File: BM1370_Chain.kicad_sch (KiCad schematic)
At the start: 30 parts, among them J6 Conn_01x06, U13 25MHz, U14 TXU0304PW, U15 MCP1824T-0802E, U16 MCP1824T-1202E

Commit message: board stakup updated and schematic is updated
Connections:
- net BM1370-1/BI: no longer R47.2
- net BM1370-1/CLKI: now also R50.2; no longer U13.3 (Out)
- net BM1370-1/CLKO: now also R52.1; no longer R50.1
- net BM1370-2/CLKI: now also R52.2; no longer R50.2
- net BM1370-2/CLKO: now also R54.1; no longer R52.1
- net BM1370-3/CLKI: now also R54.2; no longer R52.2
- net BM1370-3/CLKO: now also R56.1; no longer R54.1
- net BM1370-4/CLKI: now also R56.2; no longer R54.2
- net BM1370-4/CLKO: now also R58.1; no longer R56.1
- net BM1370-5/CLKI: now also R58.2; no longer R56.2
- net BM1370-5/CLKO: now also R59.1; no longer R58.1
- net BM1370-6/CLKI: now also R59.2; no longer R58.2
- net BM1370-6/CLKO: now also R57.1; no longer R59.1
- net BM1370-7/CLKI: now also R57.2; no longer R59.2
- net BM1370-7/CLKO: now also R55.1; no longer R57.1
- net BM1370-8/CLKI: now also R55.2; no longer R57.2
- net BM1370-8/CLKO: now also R53.1; no longer R55.1
- net BM1370-9/CLKI: now also U13.3 (Out); no longer R55.2
- net BM1370-9/CLKO: now also R50.1; no longer R53.1
- new net BM1370-9/BI: R47.2
- no-connect marks 3 -> 9
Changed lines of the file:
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@@
 	)
 	(no_connect
+		(at 138.43 135.255)
+	)
+	(no_connect
+		(at 125.095 41.275)
+	)
+	(no_connect
+		(at 125.095 43.815)
+	)
+	(no_connect
 		(at 127.635 180.34)
 	)
 	(no_connect
+		(at 138.43 138.43)
+	)
+	(no_connect
 		(at 81.915 57.785)
 	)
 	(no_connect
+		(at 138.43 147.955)
+	)
+	(no_connect
+		(at 138.43 144.78)
+	)
+	(no_connect
 		(at 70.485 180.34)
 	)
@@
 			(color 0 0 0 0.0000)
 		)
-		(property "Sheetname" "BM1370-2"
+		(property "Sheetname" "BM1370-1"
 			(at 171.45 79.9334 0)
 			(effects
@@
 		)
 		(instances
-			(project "PCIexpress_x4_full"
+			(project "PC-AXE"
 				(path "/540dc3bd-590a-41f0-90cd-0aeeeb4ef5ba/33065470-dbb7-4d39-aa86-47ade5123425"
 					(page "12")
@@
 			(color 0 0 0 0.0000)
 		)
-		(property "Sheetname" "BM1370-7"
+		(property "Sheetname" "BM1370-6"
 			(at 300.355 126.2884 0)
 			(effects
@@
 		)
 		(instances
-			(project "PCIexpress_x4_full"
+			(project "PC-AXE"
 				(path "/540dc3bd-590a-41f0-90cd-0aeeeb4ef5ba/33065470-dbb7-4d39-aa86-47ade5123425"
 					(page "17")
@@
 			(color 0 0 0 0.0000)
 		)
-		(property "Sheetname" "BM1370-3"
+		(property "Sheetname" "BM1370-2"
 			(at 203.835 79.9334 0)
 			(effects
@@
 		)
 		(instances
-			(project "PCIexpress_x4_full"
+			(project "PC-AXE"
 				(path "/540dc3bd-590a-41f0-90cd-0aeeeb4ef5ba/33065470-dbb7-4d39-aa86-47ade5123425"
 					(page "13")
@@
 		)
 		(instances
-			(project "PCIexpress_x4_full"
+			(project "PC-AXE"
 				(path "/540dc3bd-590a-41f0-90cd-0aeeeb4ef5ba/33065470-dbb7-4d39-aa86-47ade5123425"
 					(page "23")
@@
 		)
 		(instances
-			(project "PCIexpress_x4_full"
+			(project "PC-AXE"
 				(path "/540dc3bd-590a-41f0-90cd-0aeeeb4ef5ba/33065470-dbb7-4d39-aa86-47ade5123425"
 					(page "21")
@@
 		)
 		(instances
-			(project "PCIexpress_x4_full"
+			(project "PC-AXE"
 				(path "/540dc3bd-590a-41f0-90cd-0aeeeb4ef5ba/33065470-dbb7-4d39-aa86-47ade5123425"
 					(page "22")
@@
 			(color 0 0 0 0.0000)
 		)
-		(property "Sheetname" "BM1370-8"
+		(property "Sheetname" "BM1370-7"
 			(at 267.97 126.2884 0)
 			(effects
@@
 		)
 		(instances
-			(project "PCIexpress_x4_full"
+			(project "PC-AXE"
 				(path "/540dc3bd-590a-41f0-90cd-0aeeeb4ef5ba/33065470-dbb7-4d39-aa86-47ade5123425"
 					(page "18")
@@
 			(color 0 0 0 0.0000)
 		)
-		(property "Sheetname" "BM1370-9"
+		(property "Sheetname" "BM1370-8"
 			(at 235.585 126.2884 0)
 			(effects
@@
 		)
 		(instances
-			(project "PCIexpress_x4_full"
+			(project "PC-AXE"
 				(path "/540dc3bd-590a-41f0-90cd-0aeeeb4ef5ba/33065470-dbb7-4d39-aa86-47ade5123425"
 					(page "19")
@@
 			(color 0 0 0 0.0000)
 		)
-		(property "Sheetname" "BM1370-1"
+		(property "Sheetname" "BM1370-9"
 			(at 139.065 79.9334 0)
 			(effects
@@
 		)
 		(instances
-			(project "PCIexpress_x4_full"
+			(project "PC-AXE"
 				(path "/540dc3bd-590a-41f0-90cd-0aeeeb4ef5ba/33065470-dbb7-4d39-aa86-47ade5123425"
 					(page "20")
@@
 			(color 0 0 0 0.0000)
 		)
-		(property "Sheetname" "BM1370-4"
+		(property "Sheetname" "BM1370-3"
 			(at 236.22 79.9334 0)
 			(effects
@@
 		)
 		(instances
-			(project "PCIexpress_x4_full"
+			(project "PC-AXE"
 				(path "/540dc3bd-590a-41f0-90cd-0aeeeb4ef5ba/33065470-dbb7-4d39-aa86-47ade5123425"
 					(page "14")
@@
 			(color 0 0 0 0.0000)
 		)
-		(property "Sheetname" "BM1370-6"
+		(property "Sheetname" "BM1370-5"
 			(at 300.99 79.9334 0)
 			(effects
@@
 		)
 		(instances
-			(project "PCIexpress_x4_full"
+			(project "PC-AXE"
 				(path "/540dc3bd-590a-41f0-90cd-0aeeeb4ef5ba/33065470-dbb7-4d39-aa86-47ade5123425"
 					(page "16")
@@
 			(color 0 0 0 0.0000)
 		)
-		(property "Sheetname" "BM1370-5"
+		(property "Sheetname" "BM1370-4"
 			(at 268.605 79.9334 0)
 			(effects
@@
 		)
 		(instances
-			(project "PCIexpress_x4_full"
+			(project "PC-AXE"
 				(path "/540dc3bd-590a-41f0-90cd-0aeeeb4ef5ba/33065470-dbb7-4d39-aa86-47ade5123425"
 					(page "15")

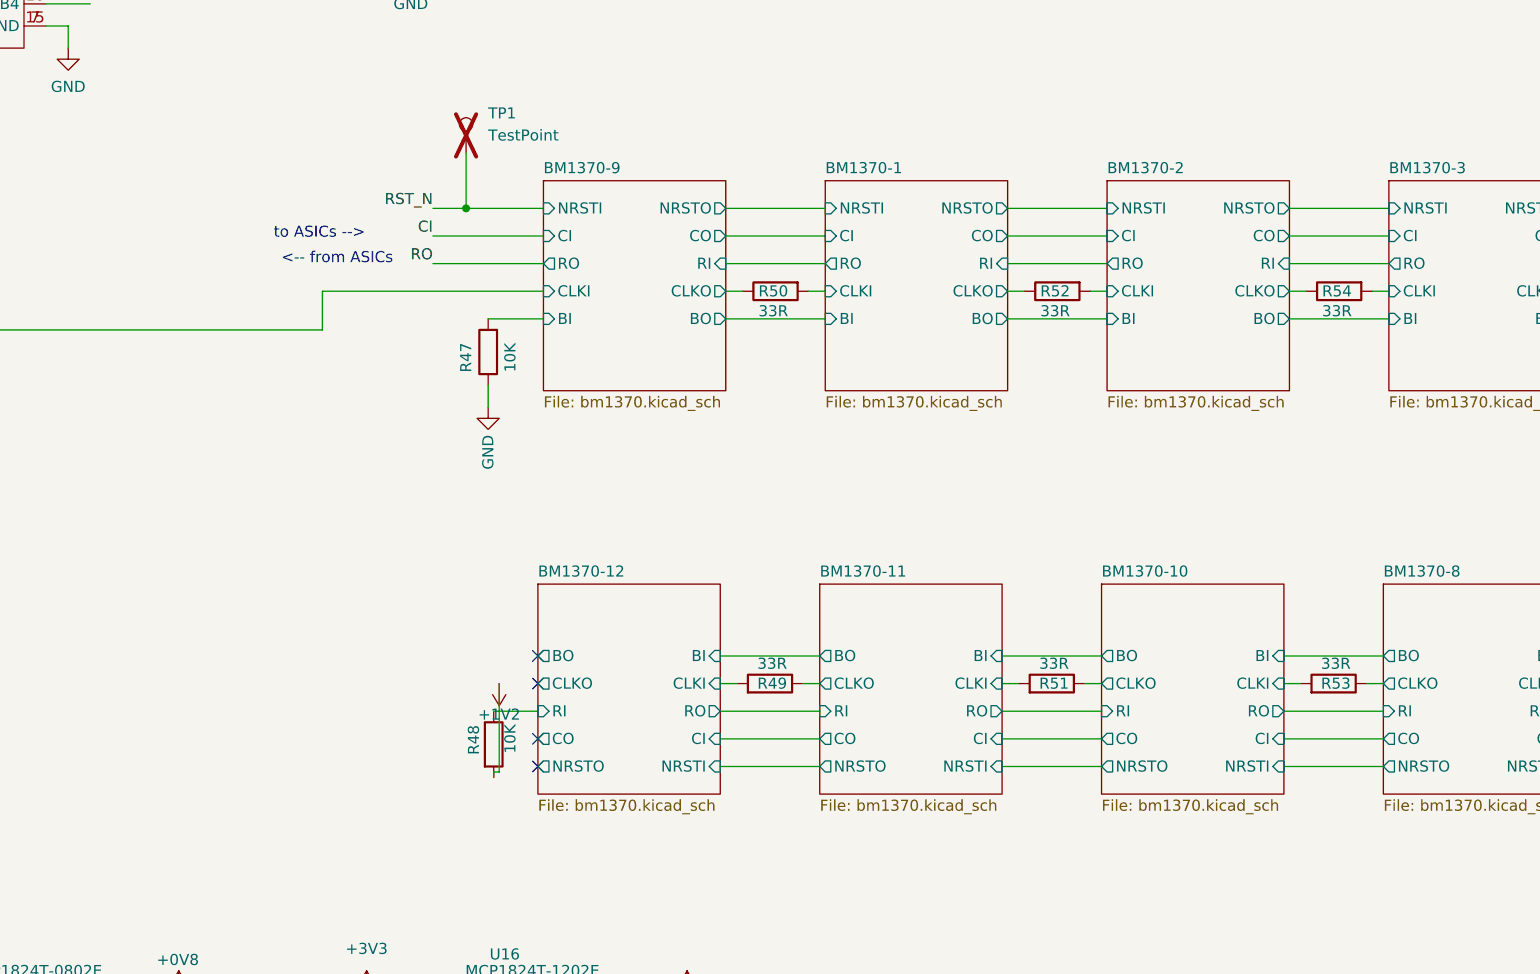
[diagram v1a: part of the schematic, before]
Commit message: updated schematic working on layout
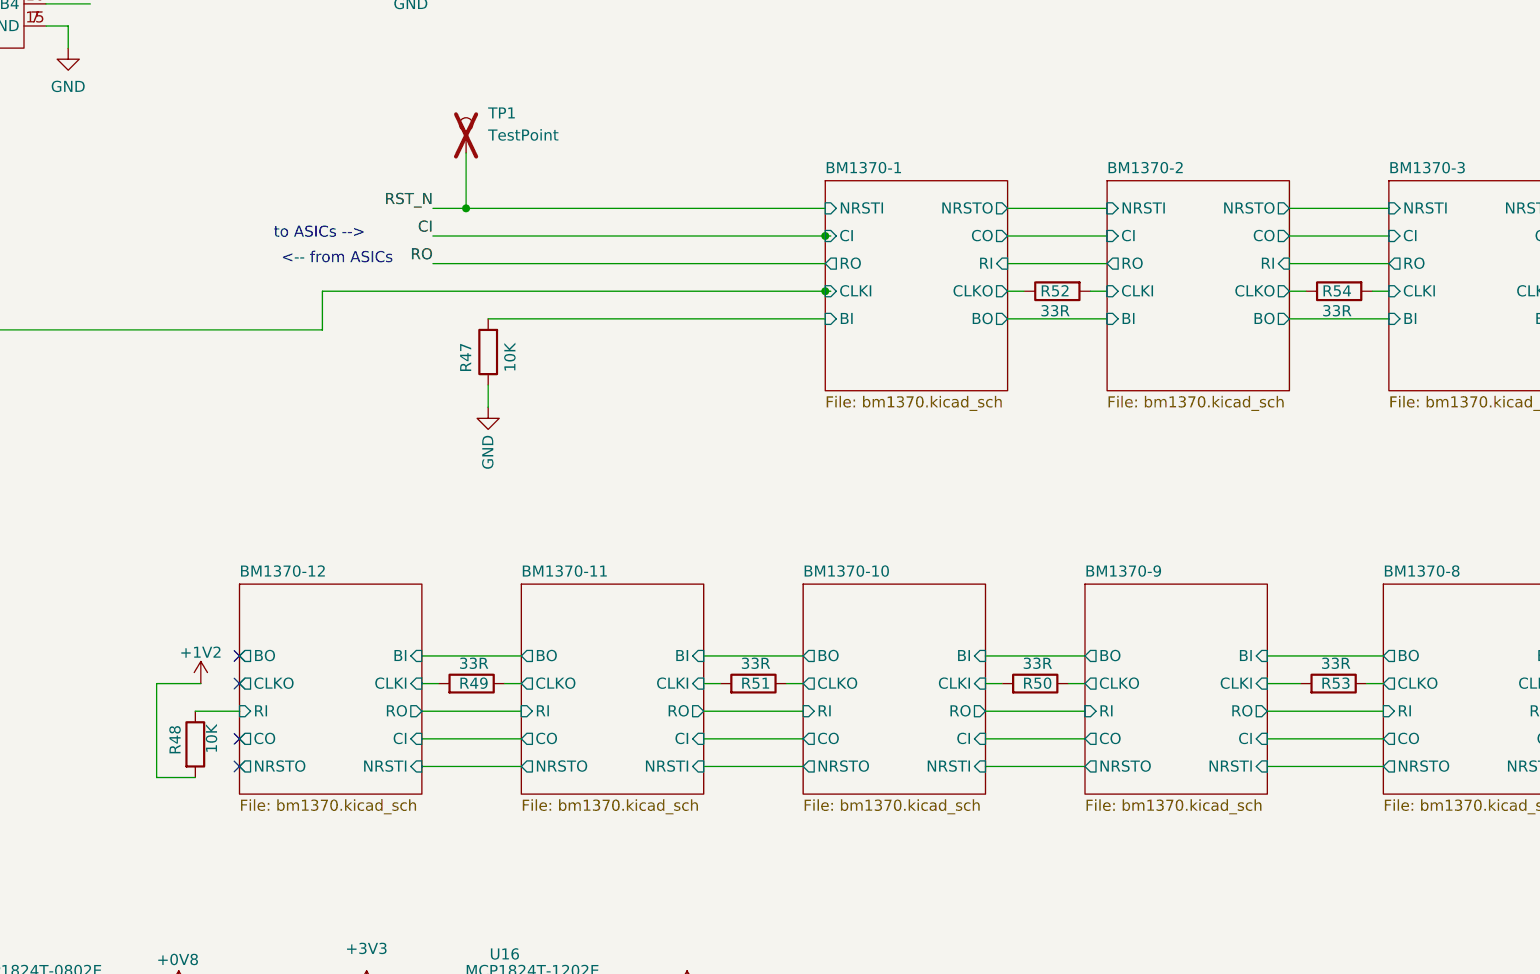
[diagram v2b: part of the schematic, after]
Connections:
- net BM1370-9/BI is gone; now on net BM1370-1/BI: R47.2
- net BM1370-1/CLKI: now also U13.3 (Out); no longer R50.2
- net BM1370-10/CLKI: now also R50.2; no longer R53.2
- net BM1370-9/CLKI: now also R53.2; no longer U13.3 (Out)
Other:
- company: (none) -> Author: Aadhi M
- title: (none) -> PC-AXE
- moved on the sheet: R48, R49, R50, R51

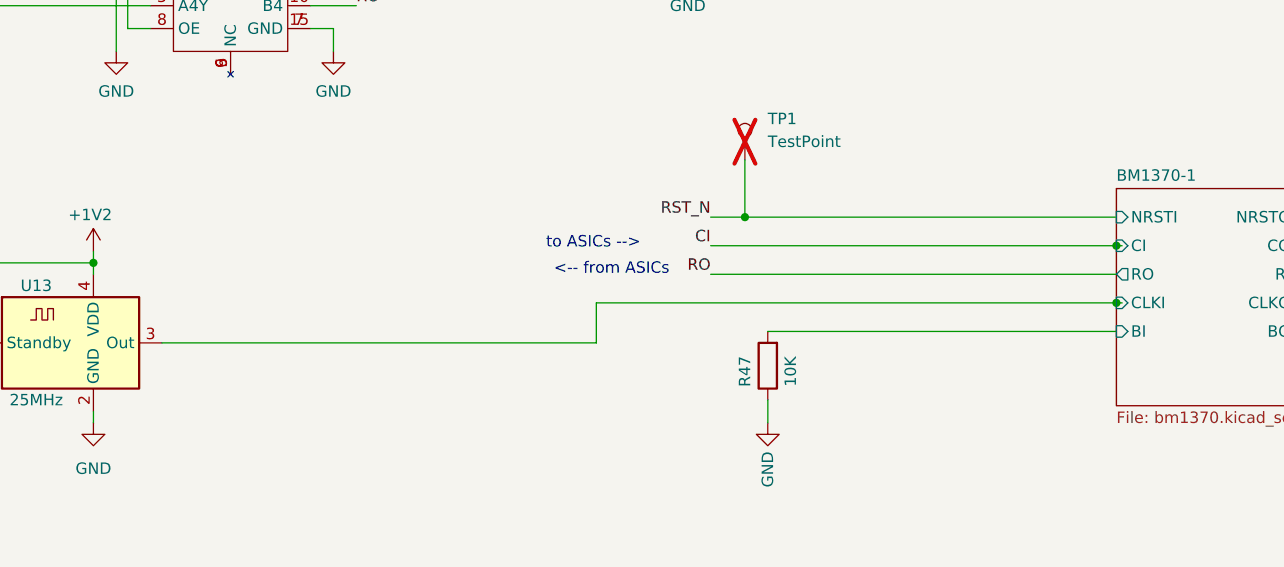
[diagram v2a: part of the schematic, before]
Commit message: Updated new layout and routing of PCB
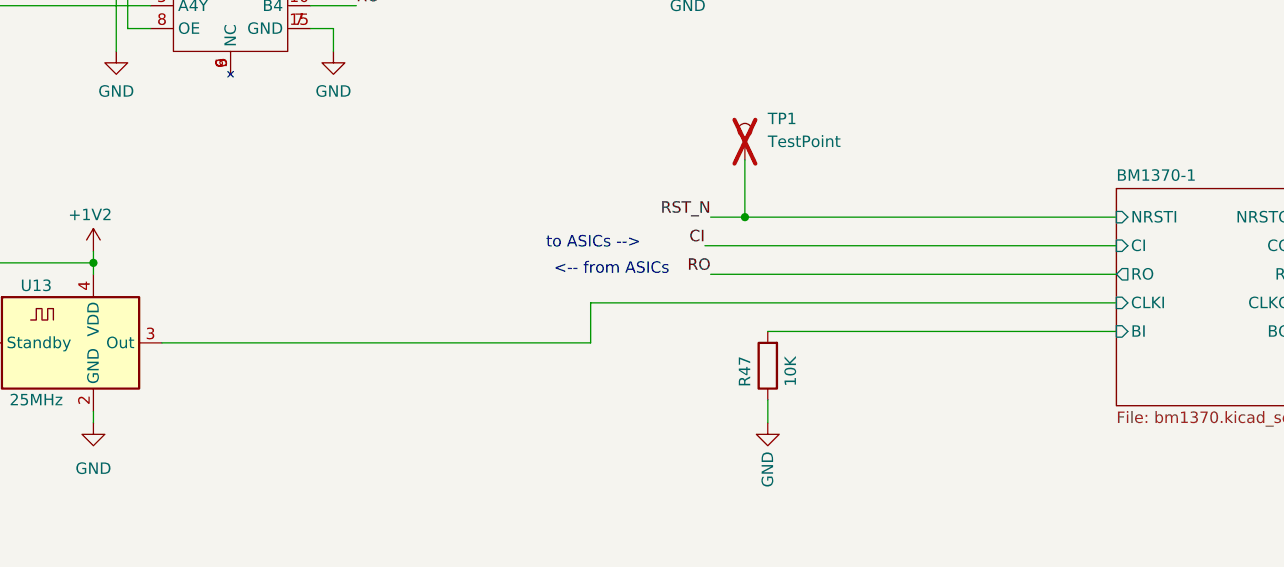
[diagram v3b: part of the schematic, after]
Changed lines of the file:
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@@
-	)
-	(junction
-		(at 171.45 93.345)
-		(diameter 0)
-		(color 0 0 0 0)
-	)
-	(junction
-		(at 171.45 86.995)
-		(diameter 0)
-		(color 0 0 0 0)
 	)
 	(junction
@@
 	(wire
 		(pts
-			(xy 113.665 93.345) (xy 171.45 93.345)
+			(xy 113.03 93.345) (xy 171.45 93.345)
 		)
 		(stroke
@@
 	(wire
 		(pts
-			(xy 65.405 97.79) (xy 113.665 97.79)
+			(xy 65.405 97.79) (xy 113.03 97.79)
 		)
 		(stroke
@@
 	(wire
 		(pts
-			(xy 171.45 86.995) (xy 172.085 86.995)
-		)
-		(stroke
-			(width 0)
-			(type default)
-		)
-	)
-	(wire
-		(pts
 			(xy 94.615 149.225) (xy 99.06 149.225)
 		)
@@
 	(wire
 		(pts
-			(xy 126.365 86.995) (xy 171.45 86.995)
+			(xy 125.73 86.995) (xy 171.45 86.995)
 		)
 		(stroke
@@
 	(wire
 		(pts
-			(xy 171.45 93.345) (xy 172.085 93.345)
-		)
-		(stroke
-			(width 0)
-			(type default)
-		)
-	)
-	(wire
-		(pts
 			(xy 335.28 93.345) (xy 321.945 93.345)
 		)
@@
 	(wire
 		(pts
-			(xy 113.665 97.79) (xy 113.665 93.345)
+			(xy 113.03 97.79) (xy 113.03 93.345)
 		)
 		(stroke
@@
 	)
 	(label "CI"
-		(at 126.365 86.995 180)
+		(at 125.73 86.995 180)
 		(effects
 			(font
